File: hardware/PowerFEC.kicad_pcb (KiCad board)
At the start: 2 copper layers, 24 x 27.9 mm, 23 parts, among them J1 B2B-XH-A, P1 105444-0001, U1 PIC16F1455, U2 AP22652, U3 ZXCT1009

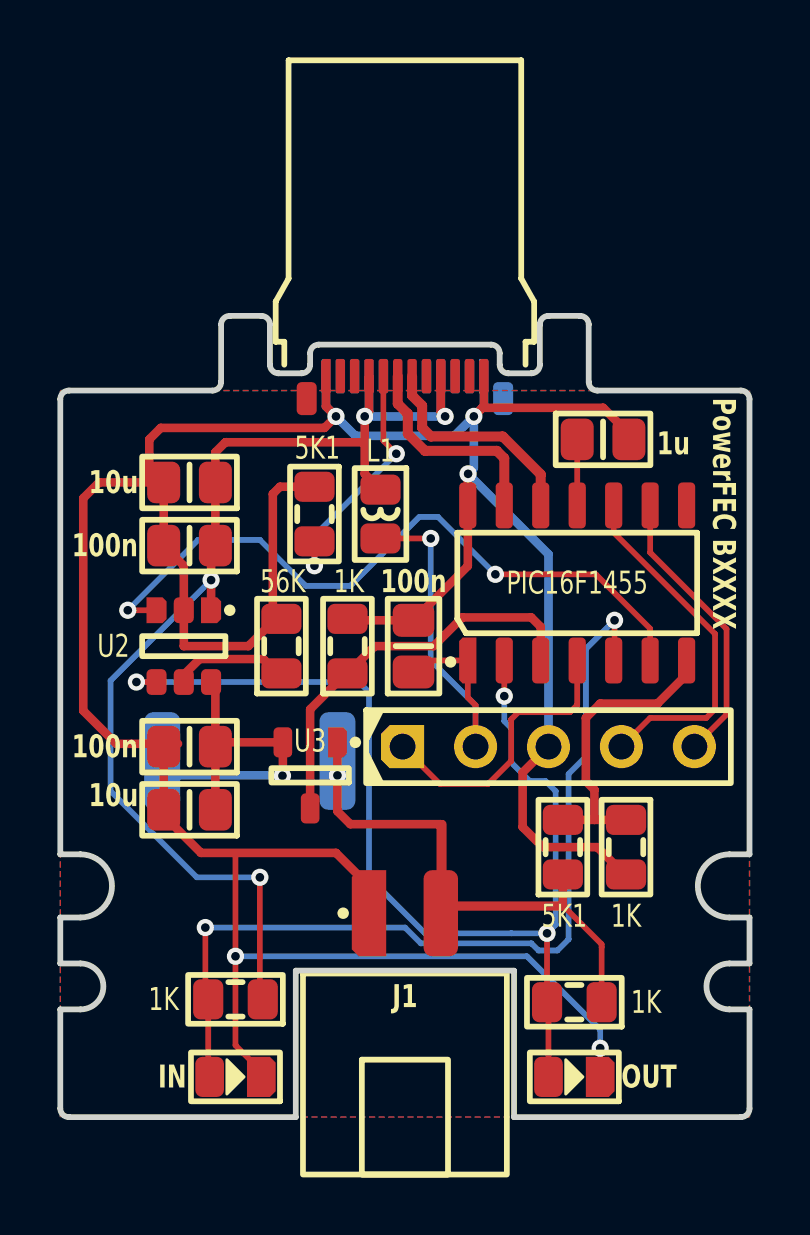
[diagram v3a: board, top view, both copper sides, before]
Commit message: Added option to control out LED by PIC (in addition to FAULT)
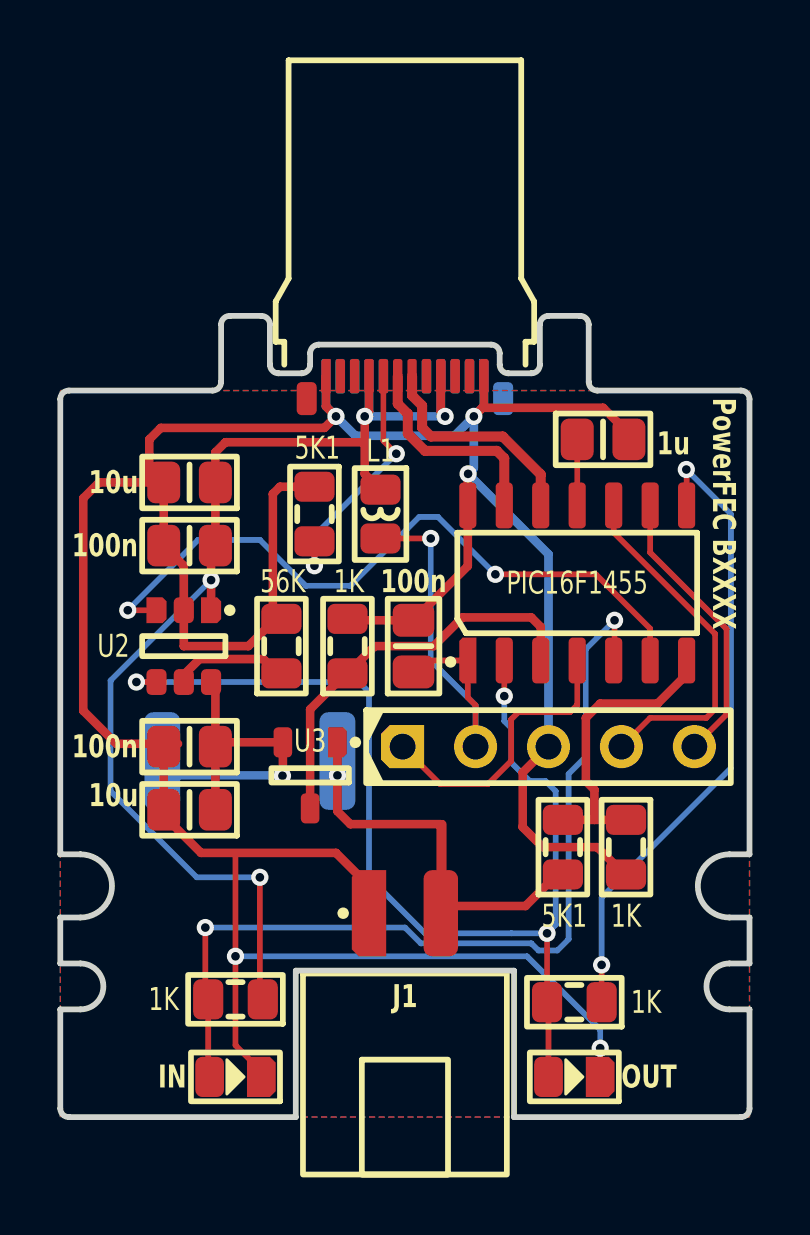
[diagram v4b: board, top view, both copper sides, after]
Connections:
- R4 pad 1: Vout -> LED_OUT_HIGH
- U1 pad 8: (no net) -> LED_OUT_HIGH
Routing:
- net LED_OUT_HIGH: track 0.00 -> 22.3 mm, vias 0 -> 2
- net Vout: track 26.8 -> 17.9 mm
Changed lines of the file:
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@@
   (net 17 "POWER_EN")
   (net 18 "POWER_FAULT")
+  (net 19 "LED_OUT_HIGH")
   (footprint "Medo64:R (0805)" (layer "F.Cu")
     (at 37.9 43.9 180)
@@
       (stroke (width 0.01) (type dash_dot)) (fill none) (layer "F.Fab"))
     (pad "1" smd roundrect (at -0.95 0 180) (size 1.05 1.4) (layers "F.Cu" "F.Paste" "F.Mask") (roundrect_rratio 0.25)
-      (net 5 "Vout") (thermal_bridge_angle 45))
+      (net 19 "LED_OUT_HIGH") (thermal_bridge_angle 45))
     (pad "2" smd roundrect (at 0.95 0 180) (size 1.05 1.4) (layers "F.Cu" "F.Paste" "F.Mask") (roundrect_rratio 0.25)
       (net 18 "POWER_FAULT") (thermal_bridge_angle 45))
@@
       (net 14 "Vadc") (thermal_bridge_angle 45))
     (pad "8" smd roundrect (at 2.7 3.81 90) (size 1.6 0.6) (layers "F.Cu" "F.Paste" "F.Mask") (roundrect_rratio 0.25)
-      (thermal_bridge_angle 45))
+      (net 19 "LED_OUT_HIGH") (thermal_bridge_angle 45))
     (pad "9" smd roundrect (at 2.7 2.54 90) (size 1.6 0.6) (layers "F.Cu" "F.Paste" "F.Mask") (roundrect_rratio 0.25)
       (net 10 "ICSP_CLK") (thermal_bridge_angle 45))
@@
   (segment (start 29.6 23.5) (end 30.275735 24.175735) (width 0.3) (layer "B.Cu") (net 4))
   (segment (start 37 28.3) (end 34.2 25.5) (width 0.3) (layer "B.Cu") (net 4))
-  (segment (start 38.85 41.98) (end 38.85 41.88) (width 0.2) (layer "F.Cu") (net 5))
   (segment (start 30.1 37.7) (end 29.65 37.25) (width 0.3) (layer "F.Cu") (net 5))
   (segment (start 33.25 40.8) (end 33.25 37.7) (width 0.3) (layer "F.Cu") (net 5))
-  (segment (start 37.5 40.55) (end 37.5 39.45) (width 0.3) (layer "F.Cu") (net 5))
-  (segment (start 33.25 40.55) (end 37.52 40.55) (width 0.3) (layer "F.Cu") (net 5))
-  (segment (start 38.85 41.88) (end 37.52 40.55) (width 0.2) (layer "F.Cu") (net 5))
   (segment (start 33.3 37.699998) (end 33.3 40.55) (width 0.3) (layer "F.Cu") (net 5))
-  (segment (start 38.85 43.9) (end 38.85 41.98) (width 0.2) (layer "F.Cu") (net 5))
+  (segment (start 37.3 39.45) (end 37.5 39.45) (width 0.3) (layer "F.Cu") (net 5))
+  (segment (start 36.2 40.55) (end 37.3 39.45) (width 0.3) (layer "F.Cu") (net 5))
+  (segment (start 33.3 40.55) (end 36.2 40.55) (width 0.3) (layer "F.Cu") (net 5))
   (segment (start 29.65 36) (end 29.65 34.85) (width 0.2) (layer "F.Cu") (net 5))
-  (segment (start 33.3 40.55) (end 37.5 40.55) (width 0.3) (layer "F.Cu") (net 5))
   (segment (start 33.25 37.7) (end 30.1 37.7) (width 0.3) (layer "F.Cu") (net 5))
   (segment (start 29.65 37.25) (end 29.65 34.85) (width 0.3) (layer "F.Cu") (net 5))
@@
   (segment (start 35.7 41.5) (end 32.7 41.5) (width 0.2) (layer "B.Cu") (net 18))
   (segment (start 30.4 32.75) (end 22.650006 32.75) (width 0.2) (layer "B.Cu") (net 18))
+  (segment (start 41.81 26.6) (end 41.81 25.36) (width 0.2) (layer "F.Cu") (net 19))
+  (segment (start 41.81 25.36) (end 41.8 25.35) (width 0.2) (layer "F.Cu") (net 19))
+  (segment (start 38.85 43.9) (end 38.85 42.6) (width 0.2) (layer "F.Cu") (net 19))
+  (via (at 41.8 25.35) (size 0.6) (drill 0.3) (layers "F.Cu" "B.Cu") (net 19))
+  (via (at 38.85 42.6) (size 0.6) (drill 0.3) (layers "F.Cu" "B.Cu") (net 19))
+  (segment (start 38.85 42.6) (end 38.85 40.251103) (width 0.2) (layer "B.Cu") (net 19))
+  (segment (start 38.85 40.251103) (end 43.35 35.751103) (width 0.2) (layer "B.Cu") (net 19))
+  (segment (start 43.35 26.9) (end 41.8 25.35) (width 0.2) (layer "B.Cu") (net 19))
+  (segment (start 43.35 35.751103) (end 43.35 26.9) (width 0.2) (layer "B.Cu") (net 19))
   (zone (net 4) (net_name "GND") (layers "F&B.Cu") (hatch edge 0.5)
     (connect_pads no (clearance 0.3))

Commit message: Updated USB edge connector designator
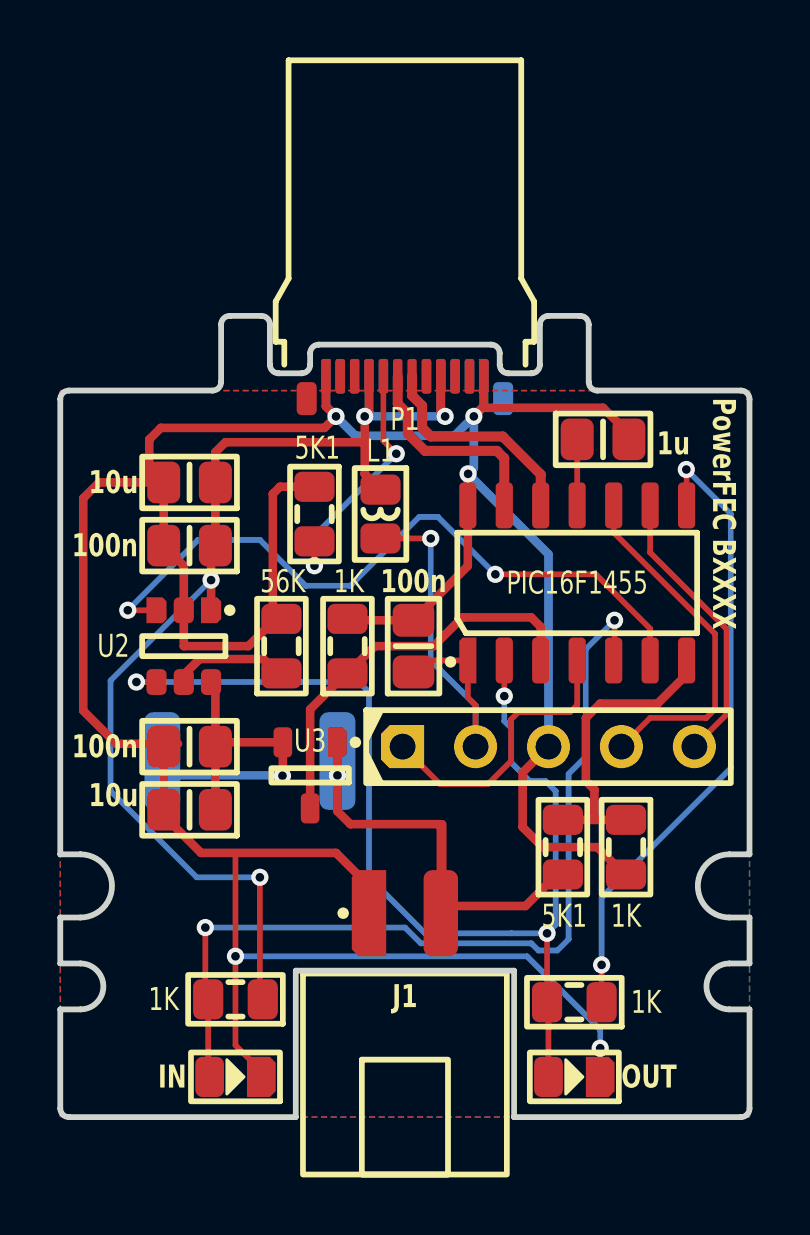
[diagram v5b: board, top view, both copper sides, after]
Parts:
- P1: footprint Medo64:P USB C 3.2 Edge (24w) -> Medo64:J USB C 3.2 Edge (24w)
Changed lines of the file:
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@@
     )
   )
-  (footprint "Medo64:P USB C 3.2 Edge (24w)" locked (layer "F.Cu")
+  (footprint "Medo64:J USB C 3.2 Edge (24w)" locked (layer "F.Cu")
     (at 32 22)
     (descr "Molex 1054440001")
     (attr smd)
-    (fp_text reference "P1" (at 0 -1.7) (layer "F.SilkS") hide
+    (fp_text reference "P1" (at 0 1.6) (layer "F.SilkS")
         (effects (font (size 0.8 0.6) (thickness 0.15)))
     )
@@
         (effects (font (size 0.8 0.6) (thickness 0.15)))
     )
-    (fp_text user "RX1+" (at -2.25 -0.8) (layer "B.Fab" knockout)
+    (fp_text user "Sbu2" (at -0.75 -0.8) (layer "B.Fab" knockout)
         (effects (font (size 0.13 0.07) (thickness 0.01)))
     )
-    (fp_text user "Vconn" (at 0.75 -0.8) (layer "B.Fab" knockout)
+    (fp_text user "TX2+" (at 2.25 -0.8) (layer "B.Fab" knockout)
+        (effects (font (size 0.13 0.07) (thickness 0.01)))
+    )
+    (fp_text user "RX1-" (at -1.75 -0.8) (layer "B.Fab" knockout)
+        (effects (font (size 0.13 0.07) (thickness 0.01)))
+    )
+    (fp_text user "TX2-" (at 1.75 -0.8) (layer "B.Fab" knockout)
+        (effects (font (size 0.13 0.07) (thickness 0.01)))
+    )
+    (fp_text user "RX1+" (at -2.25 -0.8) (layer "B.Fab" knockout)
         (effects (font (size 0.13 0.07) (thickness 0.01)))
     )
@@
         (effects (font (size 0.13 0.07) (thickness 0.01) bold))
     )
-    (fp_text user "RX1-" (at -1.75 -0.8) (layer "B.Fab" knockout)
-        (effects (font (size 0.13 0.07) (thickness 0.01)))
+    (fp_text user "Vbus" (at -1.25 -0.8) (layer "B.Fab" knockout)
+        (effects (font (size 0.13 0.07) (thickness 0.01) bold))
     )
-    (fp_text user "Sbu2" (at -0.75 -0.8) (layer "B.Fab" knockout)
-        (effects (font (size 0.13 0.07) (thickness 0.01)))
+    (fp_text user "GND" (at 2.75 -0.8) (layer "B.Fab" knockout)
+        (effects (font (size 0.13 0.07) (thickness 0.01) bold))
     )
     (fp_text user "Vbus" (at 1.25 -0.8) (layer "B.Fab" knockout)
         (effects (font (size 0.13 0.07) (thickness 0.01) bold))
     )
-    (fp_text user "TX2-" (at 1.75 -0.8) (layer "B.Fab" knockout)
+    (fp_text user "Vconn" (at 0.75 -0.8) (layer "B.Fab" knockout)
         (effects (font (size 0.13 0.07) (thickness 0.01)))
-    )
-    (fp_text user "TX2+" (at 2.25 -0.8) (layer "B.Fab" knockout)
-        (effects (font (size 0.13 0.07) (thickness 0.01)))
-    )
-    (fp_text user "GND" (at 2.75 -0.8) (layer "B.Fab" knockout)
-        (effects (font (size 0.13 0.07) (thickness 0.01) bold))
-    )
-    (fp_text user "Vbus" (at -1.25 -0.8) (layer "B.Fab" knockout)
-        (effects (font (size 0.13 0.07) (thickness 0.01) bold))
     )
     (fp_text user "GND" (at 2.75 -0.6) (layer "F.Fab" knockout)
         (effects (font (size 0.13 0.07) (thickness 0.01) bold))
-    )
-    (fp_text user "TX1+" (at -2.25 -0.6) (layer "F.Fab" knockout)
-        (effects (font (size 0.13 0.07) (thickness 0.01)))
-    )
-    (fp_text user "TX1-" (at -1.75 -0.6) (layer "F.Fab" knockout)
-        (effects (font (size 0.13 0.07) (thickness 0.01)))
     )
     (fp_text user "D-" (at 0.25 -0.6) (layer "F.Fab" knockout)
@@
         (effects (font (size 0.13 0.07) (thickness 0.01)))
     )
-    (fp_text user "CC" (at -0.75 -0.6) (layer "F.Fab" knockout)
+    (fp_text user "RX2-" (at 1.75 -0.6) (layer "F.Fab" knockout)
+        (effects (font (size 0.13 0.07) (thickness 0.01)))
+    )
+    (fp_text user "Vbus" (at -1.25 -0.6) (layer "F.Fab" knockout)
+        (effects (font (size 0.13 0.07) (thickness 0.01) bold))
+    )
+    (fp_text user "D+" (at -0.25 -0.6) (layer "F.Fab" knockout)
         (effects (font (size 0.13 0.07) (thickness 0.01)))
     )
@@
         (effects (font (size 0.13 0.07) (thickness 0.01) bold))
     )
-    (fp_text user "Vbus" (at -1.25 -0.6) (layer "F.Fab" knockout)
-        (effects (font (size 0.13 0.07) (thickness 0.01) bold))
-    )
-    (fp_text user "GND" (at -2.75 -0.6) (layer "F.Fab" knockout)
-        (effects (font (size 0.13 0.07) (thickness 0.01) bold))
-    )
-    (fp_text user "D+" (at -0.25 -0.6) (layer "F.Fab" knockout)
+    (fp_text user "CC" (at -0.75 -0.6) (layer "F.Fab" knockout)
         (effects (font (size 0.13 0.07) (thickness 0.01)))
     )
@@
         (effects (font (size 0.13 0.07) (thickness 0.01)))
     )
-    (fp_text user "RX2-" (at 1.75 -0.6) (layer "F.Fab" knockout)
+    (fp_text user "GND" (at -2.75 -0.6) (layer "F.Fab" knockout)
+        (effects (font (size 0.13 0.07) (thickness 0.01) bold))
+    )
+    (fp_text user "TX1-" (at -1.75 -0.6) (layer "F.Fab" knockout)
         (effects (font (size 0.13 0.07) (thickness 0.01)))
     )
+    (fp_text user "TX1+" (at -2.25 -0.6) (layer "F.Fab" knockout)
+        (effects (font (size 0.13 0.07) (thickness 0.01)))
+    )

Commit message: Renaming connectors
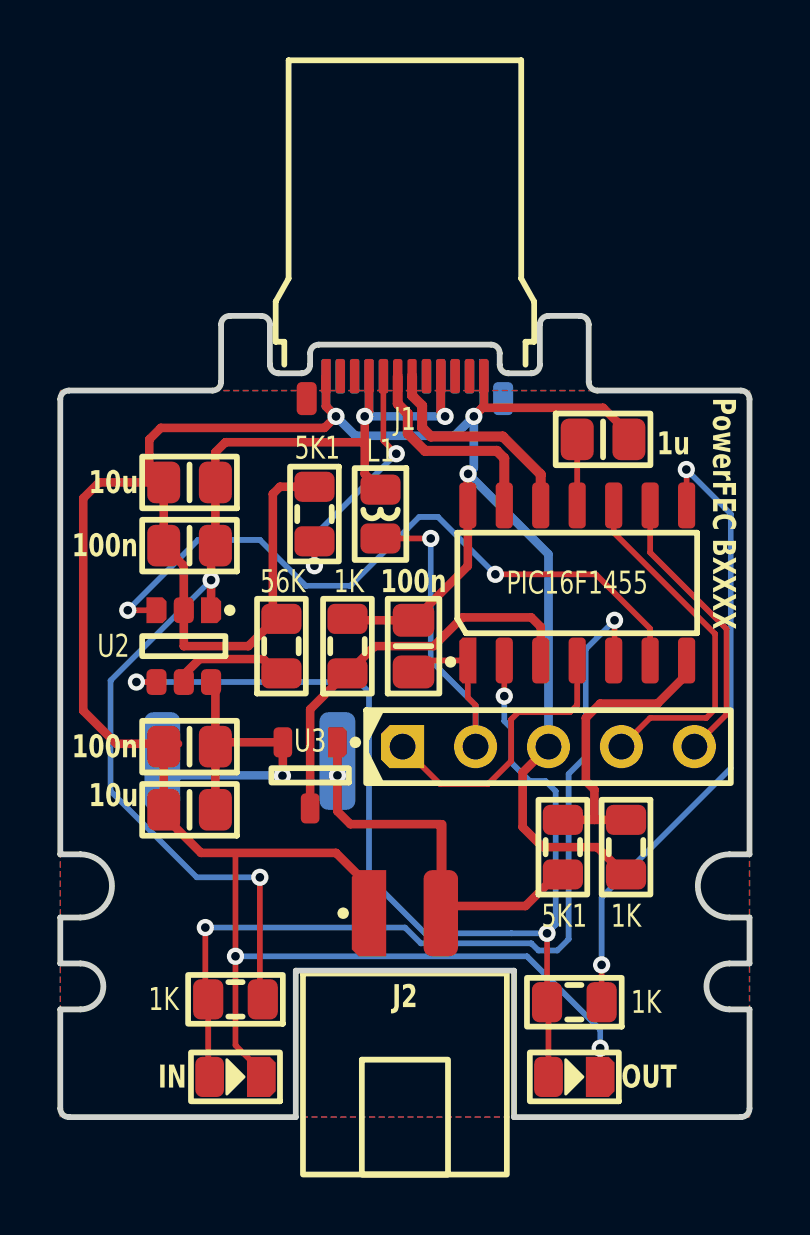
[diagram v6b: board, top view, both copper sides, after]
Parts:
- renumbered P1 to J1, J1 to J2
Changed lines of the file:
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@@
     (descr "Molex 1054440001")
     (attr smd)
-    (fp_text reference "P1" (at 0 1.6) (layer "F.SilkS")
+    (fp_text reference "J1" (at 0 1.6) (layer "F.SilkS")
         (effects (font (size 0.8 0.6) (thickness 0.15)))
     )
@@
     (descr "JST B2B-XH-A [455-B2B-XH-A-ND]")
     (attr through_hole)
-    (fp_text reference "J1" (at 0 2.9) (layer "F.SilkS")
-        (effects (font (size 0.8 0.6) (thickness 0.15) bold))
-    )
+    (fp_text reference "J2" (at 0 2.9) (layer "F.SilkS")
+        (effects (font (size 0.8 0.6) (thickness 0.15) bold))
+    )

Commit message: Added optional 18-bit ADC support
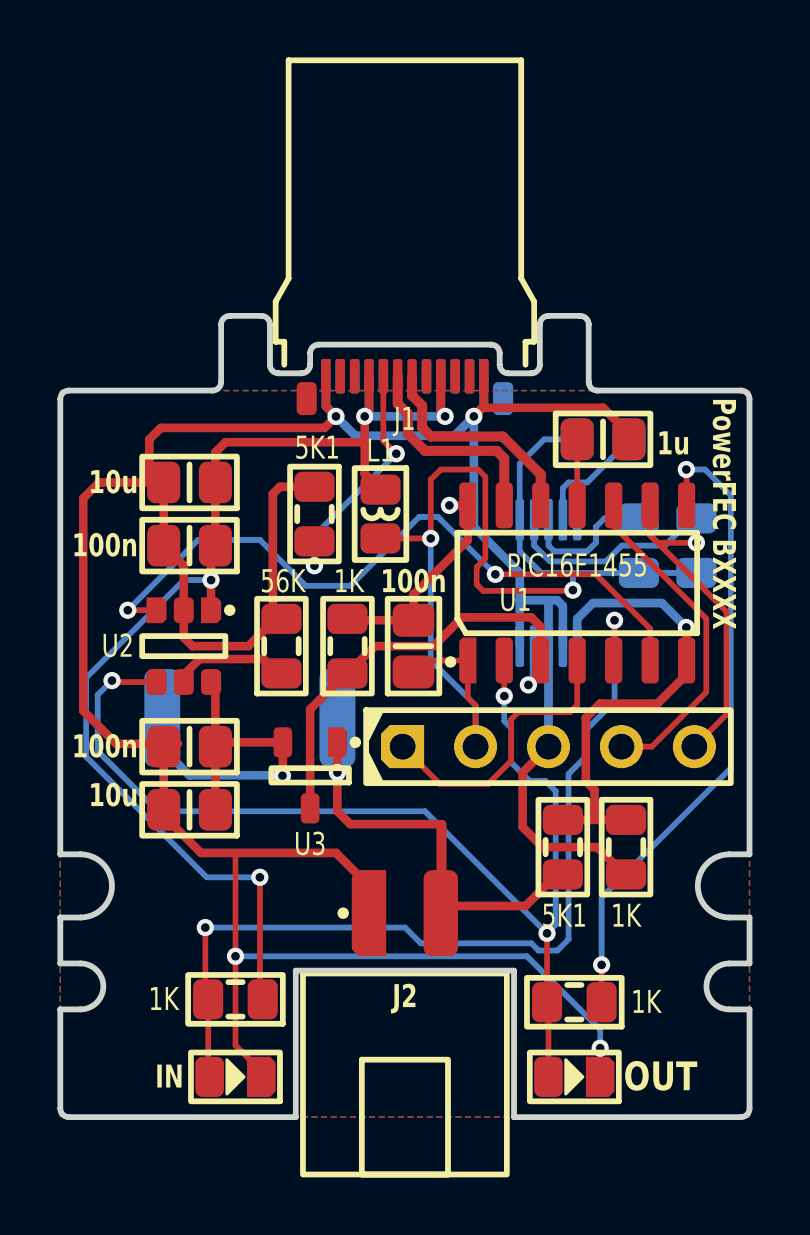
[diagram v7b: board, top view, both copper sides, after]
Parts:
- added C4: 100n, Medo64:C (0805), B.Cu at (38.9, 24.3)
- added R7: 5K1, Medo64:R (0805), B.Cu at (40.1, 28.0)
- added R8: 5K1, Medo64:R (0805), B.Cu at (42.1, 28.0)
- added U4: MCP3423, Medo64:U ADC 18bit 2ch [MCP3423] (MSOP-10), B.Cu at (37.0, 29.3)
- U1: footprint Medo64:U Micro PIC16F1455 (SOIC-14) -> Medo64:U Micro [PIC16F1455] (SOIC-14)
- U2: footprint Medo64:U CurrentLimiter AP22652 (SOT26) -> Medo64:U LoadSwitch Adjustable LatchOff EnableLow [AP22652AW6-7] (SOT23-6)
- U3: footprint Medo64:U CurrentSense ZXCT1009 (SOT23-3) -> Medo64:U Current Monitor [ZXCT1009] (SOT23-3)
- moved R1 1.50 mm to (26.6, 34.0)
- renumbered C4 to C5, C5 to C6, C6 to C7, R7 to R9
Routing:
- net 5V: track 14.4 -> 38.3 mm, vias 1 -> 2
- net ICSP_CLK: track 9.97 -> 19.8 mm, vias 0 -> 1
- net GND: track 120.7 -> 130.4 mm
- net Vadc: track 10.0 -> 16.5 mm, vias 0 -> 1
- net ICSP_DAT: track 12.4 -> 16.5 mm
- net Iadc: track 14.1 -> 16.2 mm, vias 0 -> 1
- net Vin: track 42.7 -> 43.8 mm
